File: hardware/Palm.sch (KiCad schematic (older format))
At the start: 2 parts, among them U1 VEML6075_breakout

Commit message: [prot] Add hello world code for UV sensor with nRF52 board
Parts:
- removed A1: Arduino_UNO_R3, Module:Arduino_UNO_R3, symbol MCU_Module:Arduino_UNO_R3
- added U1: Adafruit_nRF52_Feather, symbol Adafruit_nRF52_Feather:Adafruit_nRF52_Feather
- renumbered U1 to U2
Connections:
- wire segments 14 -> 17
- no-connect marks 28 -> 25
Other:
- moved on the sheet: U2
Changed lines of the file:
@@
 EESchema Schematic File Version 4
+LIBS:Palm-cache
 EELAYER 29 0
 EELAYER END
@@
 $EndDescr
 $Comp
-L MCU_Module:Arduino_UNO_R3 A1
-U 1 1 5CAF02E7
-P 3100 2500
-F 0 "A1" V 2650 1500 50  0000 L CNN
-F 1 "Arduino_UNO_R3" V 3700 2850 50  0000 L CNN
-F 2 "Module:Arduino_UNO_R3" H 3250 1450 50  0001 L CNN
-F 3 "https://www.arduino.cc/en/Main/arduinoBoardUno" H 2900 3550 50  0001 C CNN
-	1    3100 2500
-	0    1    1    0
+L Sensor_UV:VEML6075_breakout U2
+U 1 1 5CAF1352
+P 3050 1400
+F 0 "U2" H 3350 1650 50  0000 R CNN
+F 1 "VEML6075_breakout" H 2900 1150 50  0000 R CNN
+F 2 "" H 3050 1400 50  0001 C CNN
+F 3 "" H 3050 1400 50  0001 C CNN
+	1    3050 1400
+	-1   0    0    -1
 $EndComp
 $Comp
-L Sensor_UV:VEML6075_breakout U1
-U 1 1 5CAF1352
-P 2700 3650
-F 0 "U1" V 3000 3850 50  0000 R CNN
-F 1 "VEML6075_breakout" V 2350 4000 50  0000 R CNN
-F 2 "" H 2700 3650 50  0001 C CNN
-F 3 "" H 2700 3650 50  0001 C CNN
-	1    2700 3650
-	0    1    -1   0
+L Adafruit_nRF52_Feather:Adafruit_nRF52_Feather U1
+U 1 1 5CB07E1A
+P 1750 1900
+F 0 "U1" H 2150 2850 50  0000 C CNN
+F 1 "Adafruit_nRF52_Feather" H 2150 1000 50  0000 C CNN
+F 2 "" H 1600 1750 50  0001 C CNN
+F 3 "" H 1600 1750 50  0001 C CNN
+	1    1750 1900
+	-1   0    0    -1
 $EndComp
 Wire Wire Line
-	4100 2400 4300 2400
+	1800 900  1800 750
 Wire Wire Line
-	2700 3000 2700 3150
+	1800 750  2450 750
+Wire Wire Line
+	3150 750  3150 1100
 $Comp
 L power:+5V #PWR0101
-U 1 1 5CAF70B7
-P 4300 2100
-F 0 "#PWR0101" H 4300 1950 50  0001 C CNN
-F 1 "+5V" H 4315 2273 50  0000 C CNN
-F 2 "" H 4300 2100 50  0001 C CNN
-F 3 "" H 4300 2100 50  0001 C CNN
-	1    4300 2100
+U 1 1 5CB11965
+P 2450 750
+F 0 "#PWR0101" H 2450 600 50  0001 C CNN
+F 1 "+5V" H 2465 923 50  0000 C CNN
+F 2 "" H 2450 750 50  0001 C CNN
+F 3 "" H 2450 750 50  0001 C CNN
+	1    2450 750
+	1    0    0    -1
+$EndComp
+Wire Wire Line
+	3150 1700 3150 2950
+Wire Wire Line
+	3150 2950 2900 2950
+Wire Wire Line
+	1900 2950 1900 2850
+$Comp
+L power:GND #PWR0102
+U 1 1 5CB12731
+P 2500 2950
+F 0 "#PWR0102" H 2500 2700 50  0001 C CNN
+F 1 "GND" H 2505 2777 50  0000 C CNN
+F 2 "" H 2500 2950 50  0001 C CNN
+F 3 "" H 2500 2950 50  0001 C CNN
+	1    2500 2950
+	1    0    0    -1
+$EndComp
+Connection ~ 2500 2950
+Wire Wire Line
+	2500 2950 1900 2950
+Wire Wire Line
+	2300 1450 2500 1450
+Wire Wire Line
+	2500 1450 2500 1550
+Wire Wire Line
+	2500 1550 2700 1550
+Wire Wire Line
+	2700 1450 2600 1450
+Wire Wire Line
+	2600 1450 2600 1500
+Wire Wire Line
+	2600 1500 2300 1500
+Wire Wire Line
+	2300 1500 2300 1550
+NoConn ~ 1200 1150
+NoConn ~ 1200 1250
+NoConn ~ 1200 1350
+NoConn ~ 1200 1450
+NoConn ~ 1200 1550
+NoConn ~ 1200 1650
+NoConn ~ 1200 1750
+NoConn ~ 1200 1850
+NoConn ~ 1200 1950
+NoConn ~ 1200 2050
+NoConn ~ 1200 2150
+NoConn ~ 1200 2250
+NoConn ~ 1200 2450
+NoConn ~ 1200 2550
+NoConn ~ 1200 2650
+NoConn ~ 2300 2500
+NoConn ~ 2300 2250
+NoConn ~ 2300 2150
+NoConn ~ 2300 2050
+NoConn ~ 2300 1950
+NoConn ~ 2300 1850
+NoConn ~ 2300 1750
+NoConn ~ 2300 1650
+NoConn ~ 2950 1100
+$Comp
+L power:PWR_FLAG #FLG0101
+U 1 1 5CB15271
+P 2850 750
+F 0 "#FLG0101" H 2850 825 50  0001 C CNN
+F 1 "PWR_FLAG" H 2850 923 50  0000 C CNN
+F 2 "" H 2850 750 50  0001 C CNN
+F 3 "~" H 2850 750 50  0001 C CNN
+	1    2850 750
 	1    0    0    -1
 $EndComp
 $Comp
-L power:GND #PWR0103
-U 1 1 5CAF7E45
-P 1900 3750
-F 0 "#PWR0103" H 1900 3500 50  0001 C CNN
-F 1 "GND" H 1905 3577 50  0000 C CNN
-F 2 "" H 1900 3750 50  0001 C CNN
-F 3 "" H 1900 3750 50  0001 C CNN
-	1    1900 3750
-	1    0    0    -1
+L power:PWR_FLAG #FLG0102
+U 1 1 5CB15ADC
+P 2900 2950
+F 0 "#FLG0102" H 2900 3025 50  0001 C CNN
+F 1 "PWR_FLAG" H 2900 3123 50  0000 C CNN
+F 2 "" H 2900 2950 50  0001 C CNN
+F 3 "~" H 2900 2950 50  0001 C CNN
+	1    2900 2950
+	-1   0    0    1
 $EndComp
+Connection ~ 2900 2950
 Wire Wire Line
-	2000 2600 1900 2600
-NoConn ~ 2400 2000
-NoConn ~ 2500 2000
-NoConn ~ 2600 2000
-NoConn ~ 2700 2000
-NoConn ~ 2800 2000
-NoConn ~ 2900 2000
-NoConn ~ 3000 2000
-NoConn ~ 3100 2000
-NoConn ~ 3200 2000
-NoConn ~ 3300 2000
-NoConn ~ 3400 2000
-NoConn ~ 3500 2000
-NoConn ~ 3600 2000
-NoConn ~ 3700 2000
-NoConn ~ 3700 3000
-NoConn ~ 3500 3000
-NoConn ~ 3300 3000
-NoConn ~ 3100 3000
-NoConn ~ 3000 3000
-NoConn ~ 2900 3000
-NoConn ~ 2800 3000
-NoConn ~ 2000 2400
-NoConn ~ 2000 2500
-NoConn ~ 2400 3000
-NoConn ~ 2300 3000
-NoConn ~ 4100 2600
-NoConn ~ 4100 2700
-$Comp
-L power:PWR_FLAG #FLG0101
-U 1 1 5CAFADC6
-P 4300 2150
-F 0 "#FLG0101" H 4300 2225 50  0001 C CNN
-F 1 "PWR_FLAG" V 4300 2278 50  0000 L CNN
-F 2 "" H 4300 2150 50  0001 C CNN
-F 3 "~" H 4300 2150 50  0001 C CNN
-	1    4300 2150
-	0    1    1    0
-$EndComp
-$Comp
-L power:PWR_FLAG #FLG0102
-U 1 1 5CAFB749
-P 1650 2600
-F 0 "#FLG0102" H 1650 2675 50  0001 C CNN
-F 1 "PWR_FLAG" V 1650 2727 50  0000 L CNN
-F 2 "" H 1650 2600 50  0001 C CNN
-F 3 "~" H 1650 2600 50  0001 C CNN
-	1    1650 2600
-	0    -1   -1   0
-$EndComp
+	2900 2950 2500 2950
 Wire Wire Line
-	1900 2600 1650 2600
-Connection ~ 1900 2600
+	2850 750  3150 750
 Wire Wire Line
-	3000 3750 4300 3750
-Wire Wire Line
-	4300 3750 4300 2400
-Connection ~ 4300 2400
-Connection ~ 4300 2150
-Wire Wire Line
-	4300 2150 4300 2100
-Wire Wire Line
-	4300 2150 4300 2400
-Wire Wire Line
-	2650 3300 2600 3300
-Wire Wire Line
-	2600 3000 2600 3300
-Wire Wire Line
-	2550 3300 2550 3150
-Wire Wire Line
-	2550 3150 2700 3150
-Wire Wire Line
-	2400 3750 1900 3750
-Wire Wire Line
-	1900 2600 1900 3750
-Connection ~ 1900 3750
-NoConn ~ 3000 3550
+	2450 750  2850 750
+Connection ~ 2450 750
+Connection ~ 2850 750
+NoConn ~ 1700 900
 $EndSCHEMATC

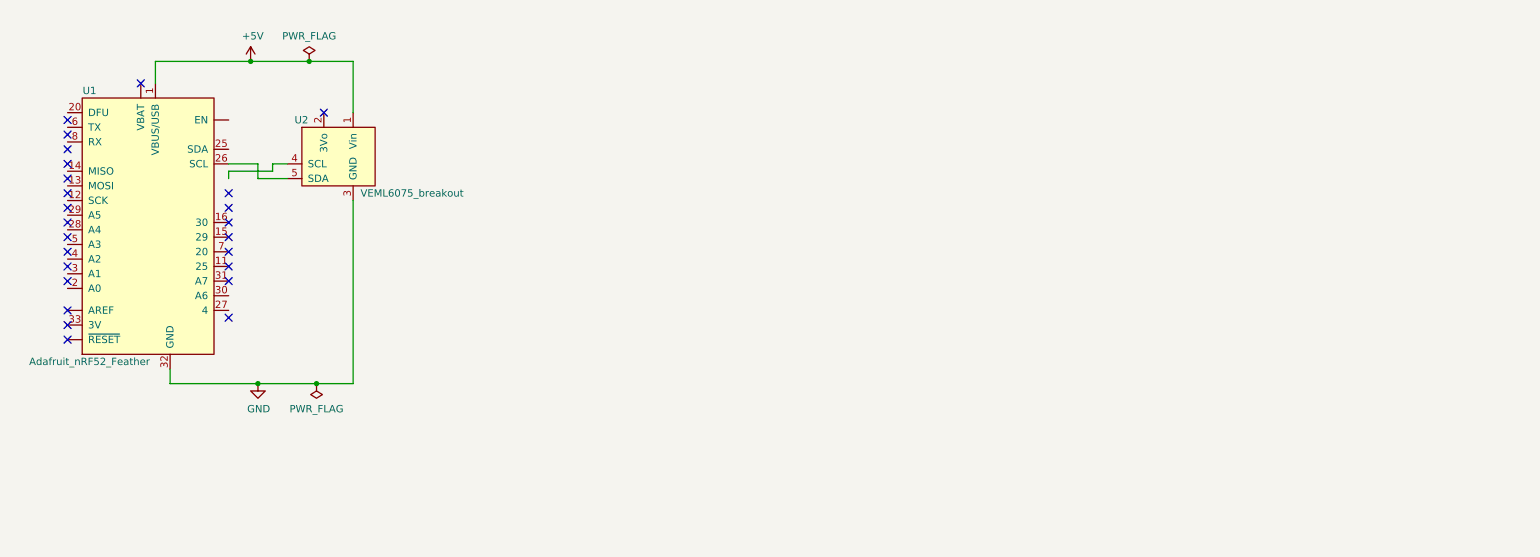
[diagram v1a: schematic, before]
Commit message: [prot] Display UV values
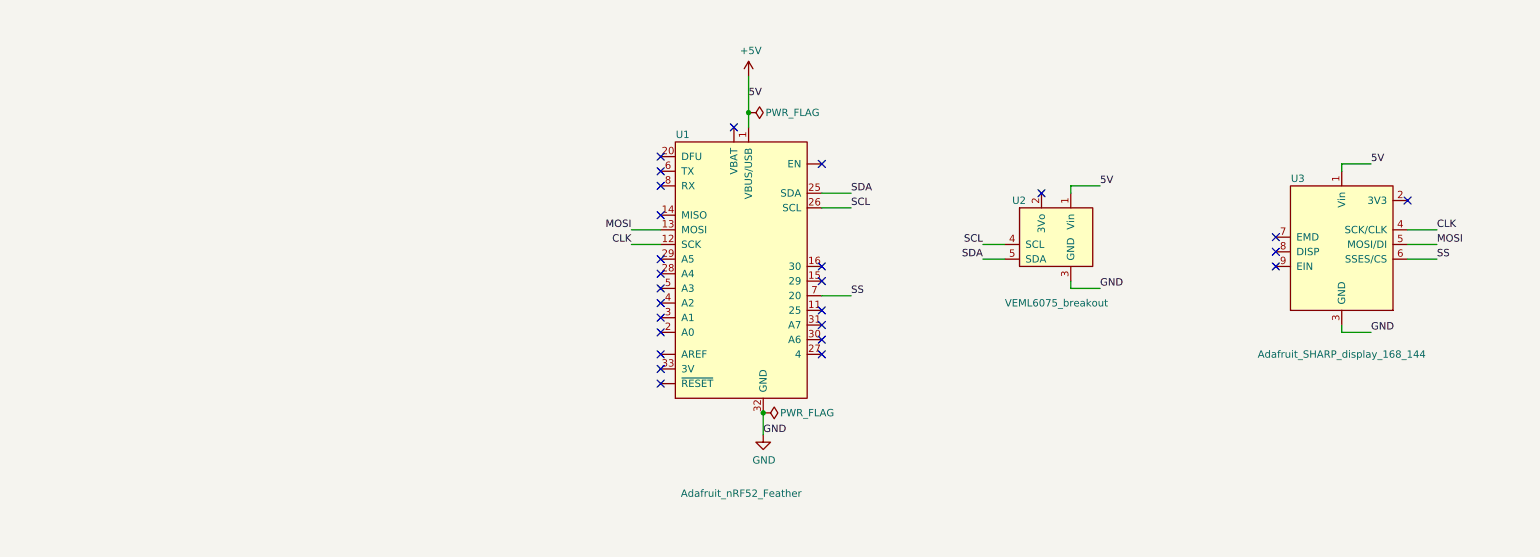
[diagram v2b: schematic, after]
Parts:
- added U3: Adafruit_SHARP_display_168_144, symbol Adafruit_SHARP_display:Adafruit_SHARP_display_168_144
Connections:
- net labels added: 5V, CLK, MOSI, SCL, SDA, SS
- wire segments 17 -> 21
- no-connect marks 25 -> 26
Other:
- moved on the sheet: U1, U2

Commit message: [prot] Display UV sensor values with a LiPo
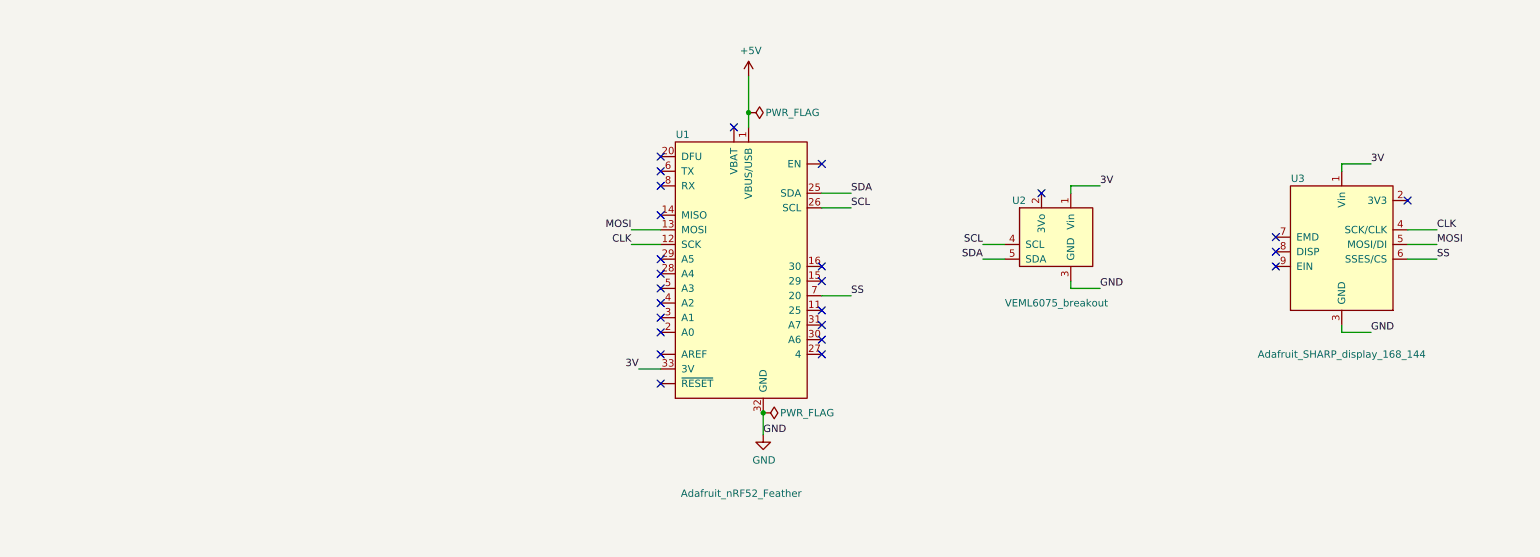
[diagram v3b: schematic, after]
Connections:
- net +5V: no longer U2.1 (Vin), U3.1 (Vin)
- net 3V: now reaches U1.33 (3V)
- net 3V: now also U2.1 (Vin), U3.1 (Vin)
- no-connect marks 26 -> 25
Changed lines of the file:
@@
 NoConn ~ 5250 2500
 NoConn ~ 5250 2750
-NoConn ~ 5250 2850
 NoConn ~ 5250 2950
 $Comp
@@
 	0    1    1    0
 $EndComp
-Text Label 5850 1000 0    50   ~ 0
-5V
+Text Label 5100 2850 2    50   ~ 0
+3V
 Text Label 5950 3300 0    50   ~ 0
 GND
@@
 	5950 3150 5950 3300
 Text Label 8250 1600 0    50   ~ 0
-5V
+3V
 $Bitmap
 Pos 2800 2050
@@
 	7450 2100 7600 2100
 Text Label 10100 1450 0    50   ~ 0
-5V
+3V
 Text Label 10100 2600 0    50   ~ 0
 GND
@@
 	5850 1100 5850 1200
 NoConn ~ 5250 2600
+Wire Wire Line
+	5250 2850 5100 2850
 $EndSCHEMATC

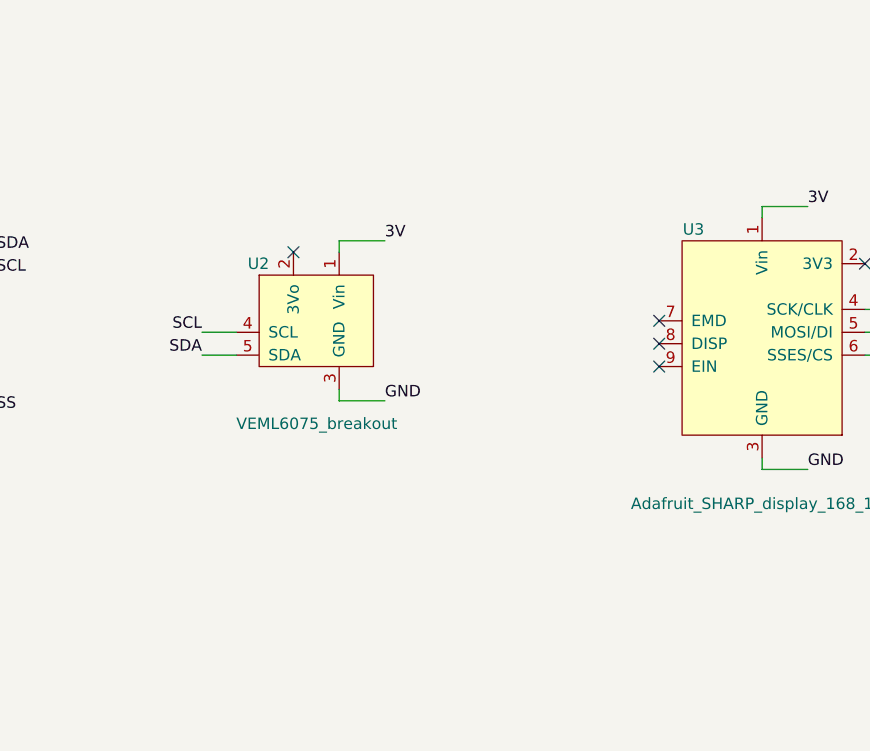
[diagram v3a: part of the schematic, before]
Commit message: [prot] Connect second sensor
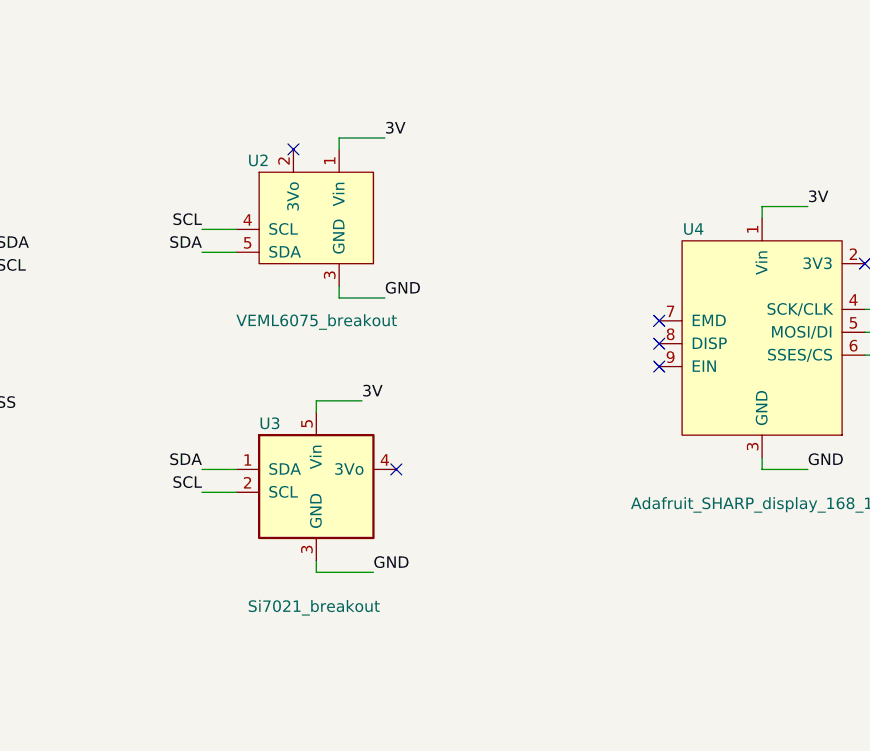
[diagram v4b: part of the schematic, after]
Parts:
- added U3: Si7021_breakout, symbol Adafruit_Si7021_breakout:Si7021_breakout
- renumbered U3 to U4
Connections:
- net 3V: now also U3.5 (Vin)
- net GND: now also U3.3 (GND)
- net SCL: now also U3.2 (SCL)
- net SDA: now also U3.1 (SDA)
- no-connect marks 25 -> 26
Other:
- moved on the sheet: U2
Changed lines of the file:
@@
 $EndComp
 $Comp
-L Adafruit_SHARP_display:Adafruit_SHARP_display_168_144 U3
+L Adafruit_SHARP_display:Adafruit_SHARP_display_168_144 U4
 U 1 1 5CB1739B
 P 9900 2050
-F 0 "U3" H 9600 2550 50  0000 C CNN
+F 0 "U4" H 9600 2550 50  0000 C CNN
 F 1 "Adafruit_SHARP_display_168_144" H 9900 1350 50  0000 C CNN
 F 2 "" H 10100 3100 50  0001 C CNN
@@
 Wire Wire Line
 	5950 3150 5950 3300
-Text Label 8250 1600 0    50   ~ 0
+Text Label 8250 1150 0    50   ~ 0
 3V
 $Bitmap
@@
 L Sensor_UV:VEML6075_breakout U2
 U 1 1 5CAF1352
-P 7950 1950
-F 0 "U2" H 8250 2200 50  0000 R CNN
-F 1 "VEML6075_breakout" H 8300 1500 50  0000 R CNN
-F 2 "" H 7950 1950 50  0001 C CNN
-F 3 "" H 7950 1950 50  0001 C CNN
-	1    7950 1950
+P 7950 1500
+F 0 "U2" H 8250 1750 50  0000 R CNN
+F 1 "VEML6075_breakout" H 8300 1050 50  0000 R CNN
+F 2 "" H 7950 1500 50  0001 C CNN
+F 3 "" H 7950 1500 50  0001 C CNN
+	1    7950 1500
 	-1   0    0    -1
 $EndComp
@@
 NoConn ~ 6350 2650
 NoConn ~ 6350 2750
-NoConn ~ 7850 1650
+NoConn ~ 7850 1200
 Wire Wire Line
-	8050 1650 8050 1600
+	8050 1200 8050 1150
 Wire Wire Line
-	8050 1600 8250 1600
+	8050 1150 8250 1150
 Wire Wire Line
-	8050 2250 8050 2300
+	8050 1800 8050 1850
 Wire Wire Line
-	8050 2300 8250 2300
-Text Label 8250 2300 0    50   ~ 0
+	8050 1850 8250 1850
+Text Label 8250 1850 0    50   ~ 0
 GND
 Text Label 6550 1650 0    50   ~ 0
@@
 Text Label 6550 1750 0    50   ~ 0
 SCL
-Text Label 7450 2000 2    50   ~ 0
+Text Label 7450 1550 2    50   ~ 0
 SCL
-Text Label 7450 2100 2    50   ~ 0
+Text Label 7450 1650 2    50   ~ 0
 SDA
 Wire Wire Line
@@
 	6350 1750 6550 1750
 Wire Wire Line
-	7450 2000 7600 2000
+	7450 1550 7600 1550
 Wire Wire Line
-	7450 2100 7600 2100
+	7450 1650 7600 1650
 Text Label 10100 1450 0    50   ~ 0
 3V
@@
 Wire Wire Line
 	5250 2850 5100 2850
+$Comp
+L Adafruit_Si7021_breakout:Si7021_breakout U3
+U 1 1 5CB56213
+P 7950 2650
+F 0 "U3" H 7700 2900 50  0000 L CNN
+F 1 "Si7021_breakout" H 7650 2100 50  0000 L CNN
+F 2 "" H 7950 2050 50  0000 C CNN
+F 3 "https://learn.adafruit.com/adafruit-si7021-temperature-plus-humidity-sensor/overview" H 7950 2450 50  0001 C CNN
+	1    7950 2650
+	1    0    0    -1
+$EndComp
+Text Label 8150 2300 0    50   ~ 0
+3V
+Text Label 8200 3050 0    50   ~ 0
+GND
+Text Label 7450 2600 2    50   ~ 0
+SDA
+Text Label 7450 2700 2    50   ~ 0
+SCL
+Wire Wire Line
+	7950 2350 7950 2300
+Wire Wire Line
+	7950 2300 8150 2300
+Wire Wire Line
+	7600 2600 7450 2600
+Wire Wire Line
+	7950 3000 7950 3050
+Wire Wire Line
+	7950 3050 8200 3050
+Wire Wire Line
+	7600 2700 7450 2700
+NoConn ~ 8300 2600
 $EndSCHEMATC

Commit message: [design] Add RGB LED to indicate UV Index
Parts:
- removed U3: Si7021_breakout, symbol Adafruit_Si7021_breakout:Si7021_breakout
- removed U4: Adafruit_SHARP_display_168_144, symbol Adafruit_SHARP_display:Adafruit_SHARP_display_168_144
- added D?: LED_BARG, symbol Device:LED_BARG
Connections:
- net labels added: BLUE, GREEN, RED
- net labels removed: CLK, MOSI, SS
- wire segments 28 -> 19
- no-connect marks 26 -> 21
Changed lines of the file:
@@
 NoConn ~ 5250 2100
 NoConn ~ 5250 2200
-NoConn ~ 5250 2300
-NoConn ~ 5250 2400
-NoConn ~ 5250 2500
 NoConn ~ 5250 2750
 NoConn ~ 5250 2950
@@
 $EndComp
 $Comp
-L Adafruit_SHARP_display:Adafruit_SHARP_display_168_144 U4
-U 1 1 5CB1739B
-P 9900 2050
-F 0 "U4" H 9600 2550 50  0000 C CNN
-F 1 "Adafruit_SHARP_display_168_144" H 9900 1350 50  0000 C CNN
-F 2 "" H 10100 3100 50  0001 C CNN
-F 3 "" H 10100 3100 50  0001 C CNN
-	1    9900 2050
-	1    0    0    -1
-$EndComp
-$Comp
 L power:PWR_FLAG #FLG0102
 U 1 1 5CB15ADC
@@
 Wire Wire Line
 	7450 1650 7600 1650
-Text Label 10100 1450 0    50   ~ 0
-3V
-Text Label 10100 2600 0    50   ~ 0
-GND
-NoConn ~ 9450 1950
-NoConn ~ 9450 2050
-NoConn ~ 9450 2150
-Text Label 10550 1900 0    50   ~ 0
-CLK
-Text Label 5050 2000 2    50   ~ 0
-CLK
-Text Label 10550 2000 0    50   ~ 0
-MOSI
-Text Label 5050 1900 2    50   ~ 0
-MOSI
-Text Label 10550 2100 0    50   ~ 0
-SS
-Text Label 6550 2350 0    50   ~ 0
-SS
-Wire Wire Line
-	10350 1900 10550 1900
-Wire Wire Line
-	10350 2000 10550 2000
-Wire Wire Line
-	10350 2100 10550 2100
-Wire Wire Line
-	9900 1500 9900 1450
-Wire Wire Line
-	9900 1450 10100 1450
-Wire Wire Line
-	9900 2550 9900 2600
-Wire Wire Line
-	9900 2600 10100 2600
-Wire Wire Line
-	6350 2350 6550 2350
-Wire Wire Line
-	5050 1900 5250 1900
-Wire Wire Line
-	5050 2000 5250 2000
-NoConn ~ 10350 1700
 Wire Wire Line
 	5850 850  5850 1100
@@
 Wire Wire Line
 	5250 2850 5100 2850
+NoConn ~ 6350 2350
+NoConn ~ 5250 2000
+NoConn ~ 5250 1900
 $Comp
-L Adafruit_Si7021_breakout:Si7021_breakout U3
-U 1 1 5CB56213
-P 7950 2650
-F 0 "U3" H 7700 2900 50  0000 L CNN
-F 1 "Si7021_breakout" H 7650 2100 50  0000 L CNN
-F 2 "" H 7950 2050 50  0000 C CNN
-F 3 "https://learn.adafruit.com/adafruit-si7021-temperature-plus-humidity-sensor/overview" H 7950 2450 50  0001 C CNN
-	1    7950 2650
+L Device:LED_BARG D?
+U 1 1 5CED4526
+P 7950 2700
+F 0 "D?" H 7950 3197 50  0000 C CNN
+F 1 "LED_BARG" H 7950 3106 50  0000 C CNN
+F 2 "" H 7950 2650 50  0001 C CNN
+F 3 "~" H 7950 2650 50  0001 C CNN
+	1    7950 2700
 	1    0    0    -1
 $EndComp
-Text Label 8150 2300 0    50   ~ 0
-3V
-Text Label 8200 3050 0    50   ~ 0
-GND
-Text Label 7450 2600 2    50   ~ 0
-SDA
-Text Label 7450 2700 2    50   ~ 0
-SCL
+Text Label 5050 2500 2    50   ~ 0
+RED
+Text Label 5050 2400 2    50   ~ 0
+GREEN
+Text Label 5050 2300 2    50   ~ 0
+BLUE
 Wire Wire Line
-	7950 2350 7950 2300
+	5050 2500 5250 2500
 Wire Wire Line
-	7950 2300 8150 2300
+	5050 2400 5250 2400
+Wire Wire Line
+	5050 2300 5250 2300
+Text Label 7600 2500 2    50   ~ 0
+RED
+Text Label 7600 2700 2    50   ~ 0
+GREEN
+Text Label 7600 2900 2    50   ~ 0
+BLUE
+Text Label 8300 2700 0    50   ~ 0
+GND
 Wire Wire Line
-	7600 2600 7450 2600
+	7600 2500 7750 2500
 Wire Wire Line
-	7950 3000 7950 3050
+	7600 2700 7750 2700
 Wire Wire Line
-	7950 3050 8200 3050
+	7600 2900 7750 2900
 Wire Wire Line
-	7600 2700 7450 2700
-NoConn ~ 8300 2600
+	8150 2700 8300 2700
 $EndSCHEMATC
